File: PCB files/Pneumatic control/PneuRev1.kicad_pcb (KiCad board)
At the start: 2 copper layers, 135.4 x 77.3 mm, 72 parts, among them J1 SIG_IN, J2 BATT_IN, J3 PNEU, U1 OPA551, U10 OPA551, U11 OPA551, U12 OPA551, U13 OPA551, U2 OPA551, U3 OPA551, U4 OPA551, U5 OPA551, U6 OPA551, U7 OPA551, U8 OPA551, U9 OPA551

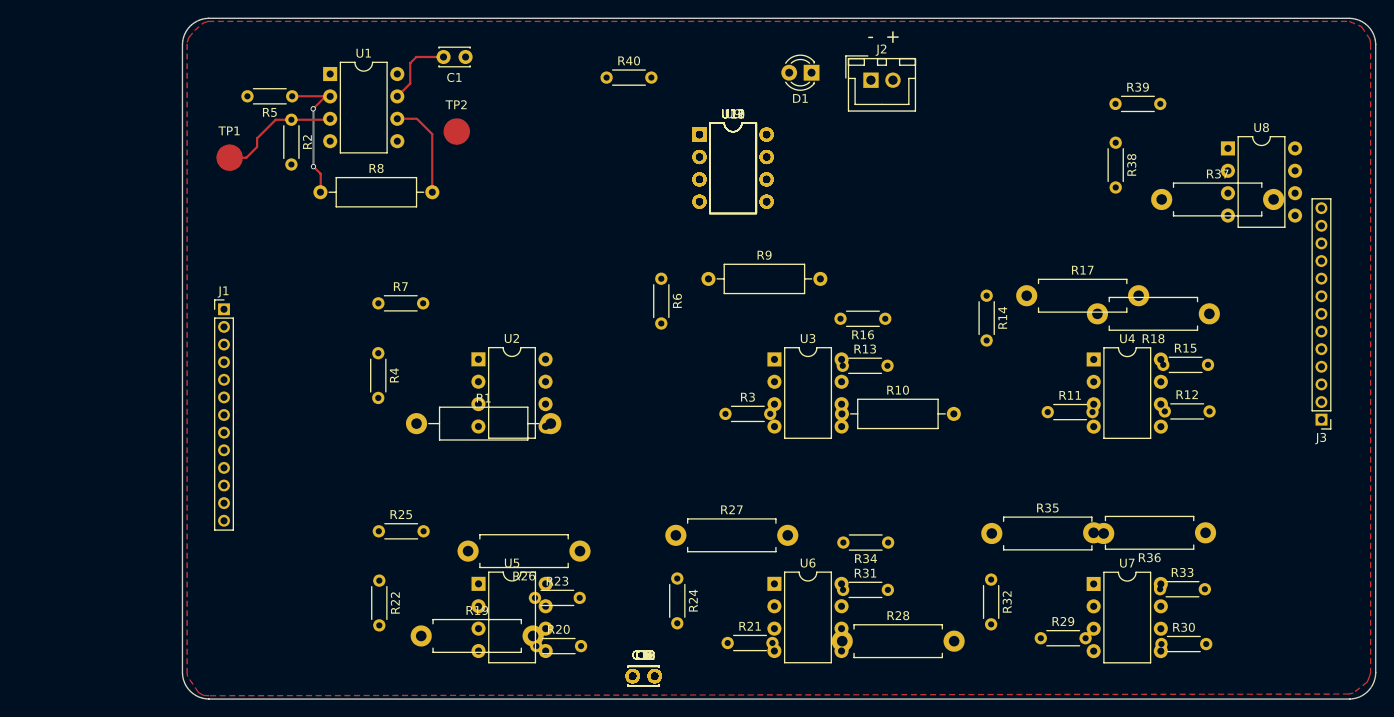
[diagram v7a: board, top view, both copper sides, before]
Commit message: 2/22/2019
-Finished board routing
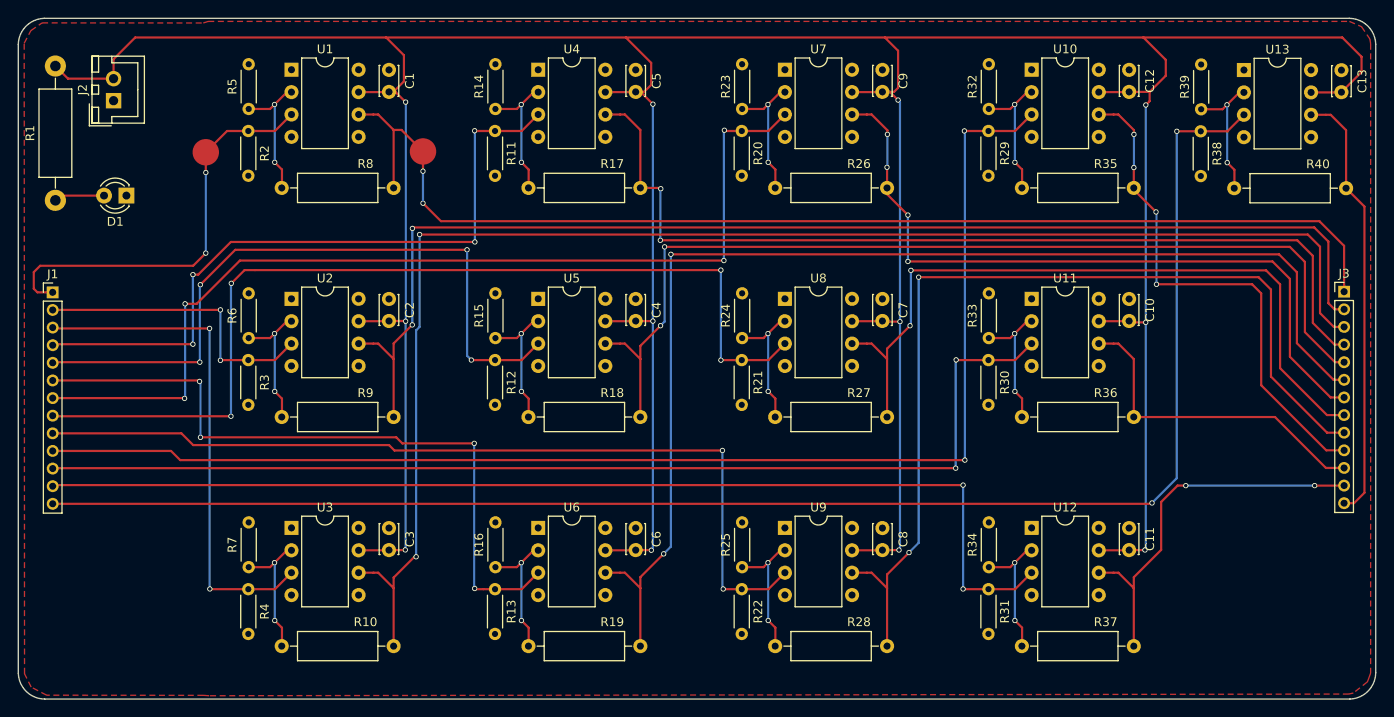
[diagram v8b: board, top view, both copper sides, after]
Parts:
- R17, R18, R19, R26, R27, R28, R35, R36, R37: footprint Resistors_THT:R_Axial_DIN0411_L9.9mm_D3.6mm_P12.70mm_Horizontal -> Resistors_THT:R_Axial_DIN0309_L9.0mm_D3.2mm_P12.70mm_Horizontal
- R40: footprint Resistors_THT:R_Axial_DIN0204_L3.6mm_D1.6mm_P5.08mm_Horizontal -> Resistors_THT:R_Axial_DIN0309_L9.0mm_D3.2mm_P12.70mm_Horizontal
- moved C13 105.8 mm to (216.0, 67.7), turned to 270 degrees
- moved C12 88.9 mm to (191.9, 67.6), turned to 270 degrees
- moved J2 86.0 mm to (76.7, 71.1), turned to 90 degrees
- moved D1 79.0 mm to (78.1, 81.9)
- moved R18 78.2 mm to (123.8, 107.0), turned to 0 degrees
- moved R12 76.2 mm to (120.0, 100.6), turned to 270 degrees
- moved R15 75.9 mm to (120.0, 98.1), turned to 90 degrees
- moved C9 74.4 mm to (163.9, 67.6), turned to 270 degrees
- moved R40 72.3 mm to (203.9, 81.1)
- moved U4 71.1 mm to (124.9, 67.6)
- moved C10 70.8 mm to (191.9, 93.6), turned to 270 degrees
- moved R11 70.4 mm to (120.0, 74.6), turned to 270 degrees
- moved R10 68.8 mm to (95.8, 133.0)
- moved C5 68.8 mm to (135.9, 67.6), turned to 270 degrees
- moved U7 68.1 mm to (152.9, 67.6)
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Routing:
- net Net-(C1-Pad2): track 8.46 -> 465.3 mm, vias 0 -> 12
- net /IN13: track 0.00 -> 177.3 mm, vias 0 -> 2
- net /PNU3: track 0.00 -> 166.4 mm, vias 0 -> 2
- net /IN10: track 0.00 -> 150.5 mm, vias 0 -> 2
- net /PNU2: track 0.00 -> 140.7 mm, vias 0 -> 2
- net /PNU6: track 0.00 -> 137.6 mm, vias 0 -> 2
- net /IN11: track 0.00 -> 125.0 mm, vias 0 -> 2
- net /IN12: track 0.00 -> 124.5 mm, vias 0 -> 2
- net /PNU1: track 11.3 -> 133.2 mm, vias 0 -> 2
- net /PNU5: track 0.00 -> 112.4 mm, vias 0 -> 2
- net /IN7: track 0.00 -> 112.2 mm, vias 0 -> 4
- net /IN8: track 0.00 -> 110.6 mm, vias 0 -> 4
- net /PNU9: track 0.00 -> 109.4 mm, vias 0 -> 2
- net /PNU4: track 0.00 -> 106.5 mm, vias 0 -> 2
- net /IN9: track 0.00 -> 101.2 mm, vias 0 -> 2
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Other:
- board size 135.4 x 77.3 mm -> 154.1 x 77.3 mm
- board text removed: "+"
- board text removed: "-"
